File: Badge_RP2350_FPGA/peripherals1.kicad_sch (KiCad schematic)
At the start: 21 parts, among them J3 Conn_01x15_Pin, J4 Conn_01x15_Pin

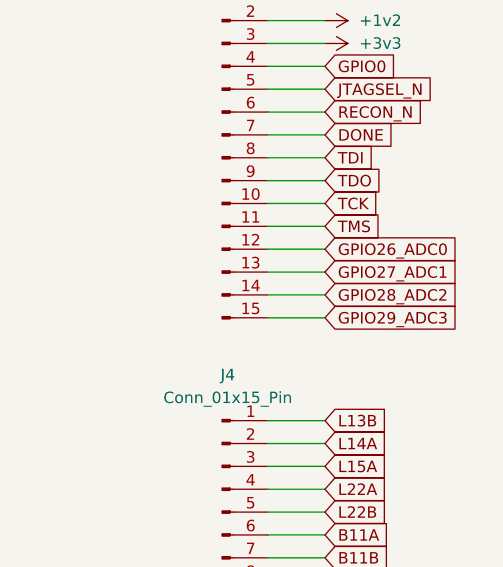
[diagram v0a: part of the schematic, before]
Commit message: Version 1.6: fix FB3 error, fix missing secondary flash pull-up, fix missing diode on battery, realign and add silkscreen
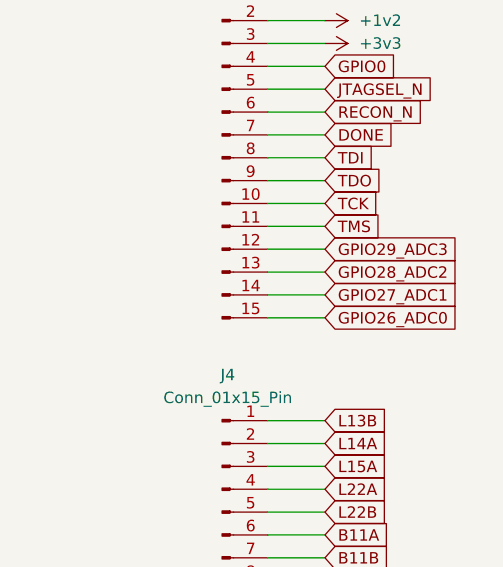
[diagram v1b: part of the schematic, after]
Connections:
- net GPIO26_ADC0: now also J3.15 (Pin_15); no longer J3.12 (Pin_12)
- net GPIO27_ADC1: now also J3.14 (Pin_14); no longer J3.13 (Pin_13)
- net GPIO28_ADC2: now also J3.13 (Pin_13); no longer J3.14 (Pin_14)
- net GPIO29_ADC3: now also J3.12 (Pin_12); no longer J3.15 (Pin_15)

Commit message: put pull up to mode1, pull down to mode0
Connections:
- net T8A: no longer names the net of J4.14 (Pin_14)
- net T8B: no longer names the net of J4.15 (Pin_15)
- no-connect marks 0 -> 2
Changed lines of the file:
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@@
 		(color 0 0 0 0)
 	)
+	(no_connect
+		(at 177.8 119.38)
+	)
+	(no_connect
+		(at 177.8 121.92)
+	)
 	(wire
 		(pts
@@
 		)
 	)
-	(global_label "T8B"
-		(shape input)
-		(at 177.8 121.92 0)
-		(fields_autoplaced yes)
-		(effects
-			(font
-				(size 1.27 1.27)
-			)
-			(justify left)
-		)
-		(property "Intersheetrefs" "${INTERSHEET_REFS}"
-			(at 184.2323 121.92 0)
-			(hide yes)
-			(show_name no)
-			(do_not_autoplace no)
-			(effects
-				(font
-					(size 1.27 1.27)
-				)
-				(justify left)
-			)
-		)
-	)
 	(global_label "B11B"
 		(shape input)
@@
 			(hide yes)
 			(show_name no)
-			(do_not_autoplace no)
-			(effects
-				(font
-					(size 1.27 1.27)
-				)
-				(justify left)
-			)
-		)
-	)
-	(global_label "T8A"
-		(shape input)
-		(at 177.8 119.38 0)
-		(fields_autoplaced yes)
-		(effects
-			(font
-				(size 1.27 1.27)
-			)
-			(justify left)
-		)
-		(property "Intersheetrefs" "${INTERSHEET_REFS}"
-			(at 184.0509 119.38 0)
-			(hide yes)
-			(show_name no)
